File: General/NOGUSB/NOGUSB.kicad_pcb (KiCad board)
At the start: 2 copper layers, 34 parts, among them J1 USB4105-GF-A, J2 SPI/I2C/CAN/DAC, J3 CAN, J4 SWD_UART, SW1 RST, SW2 DBG2, SW3 BOOT0, SW4 DBG1, U1 MAX77596ETBB+, U2 TCAN330G, U3 STM32G0B1KxTxN

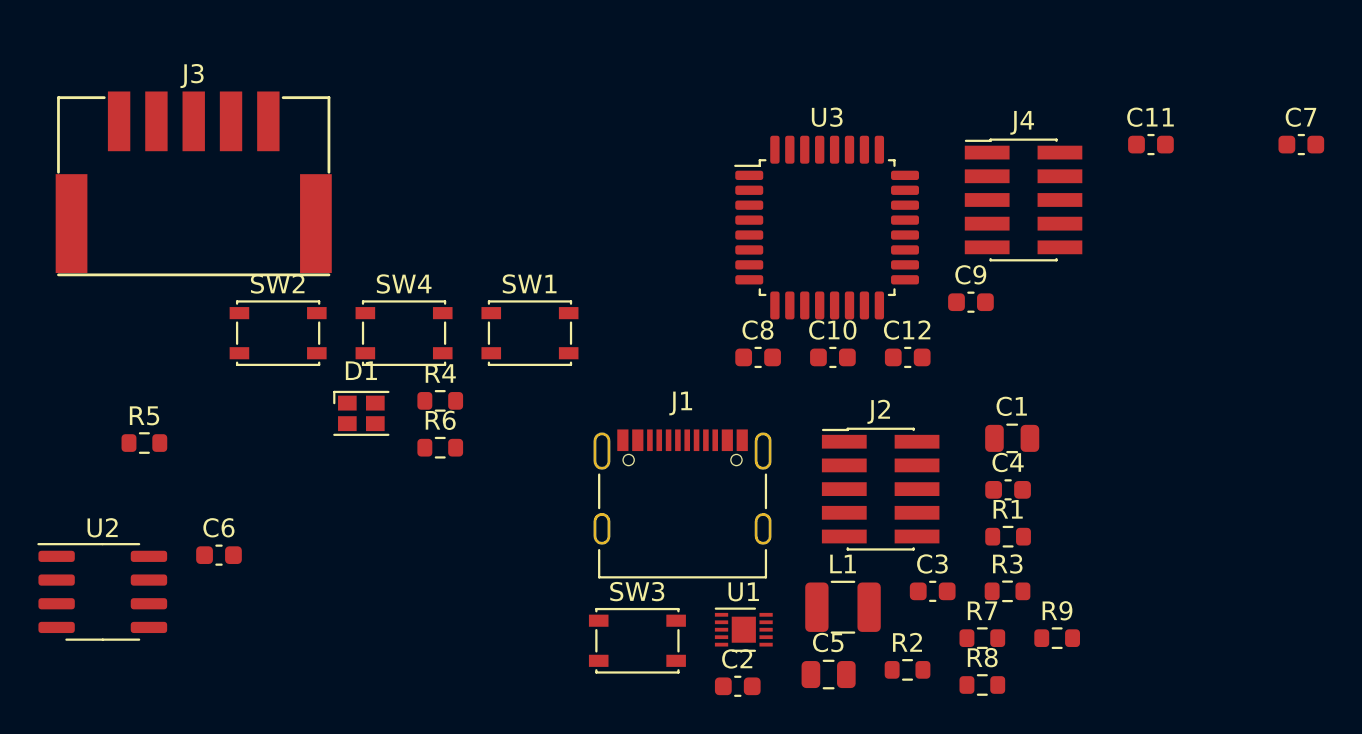
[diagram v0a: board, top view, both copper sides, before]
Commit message: finished NOGUSB layout
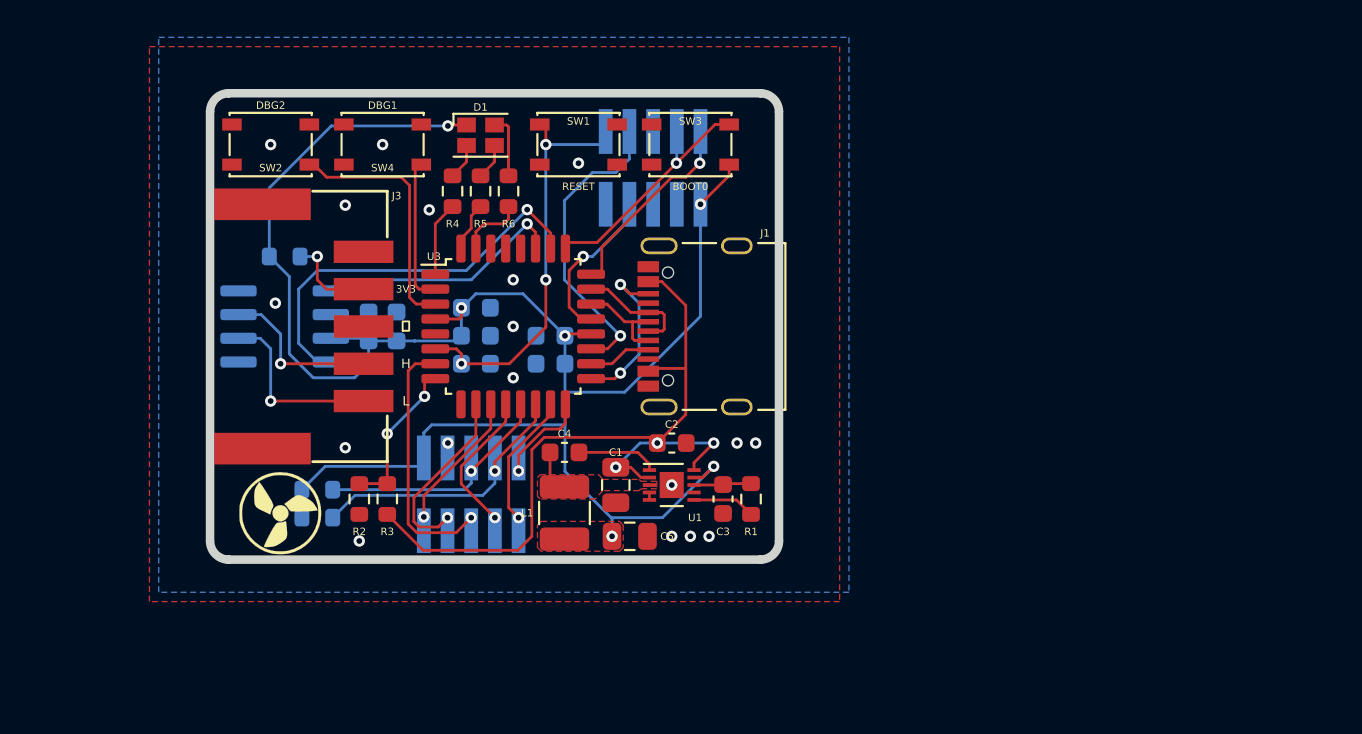
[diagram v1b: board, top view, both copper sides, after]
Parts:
- added H1: Logo, extraparts:auv_logo, F.Cu at (137.5, 110.0)
- C10, C11, C12, C6, C7, C8, C9, J2, J4, R7, R8, R9, U2: moved to B.Cu
- moved C7 49.5 mm to (143.8, 100.0), turned to 90 degrees
- moved R9 46.2 mm to (137.8, 96.2)
- moved R8 36.8 mm to (139.5, 110.2), turned to 180 degrees
- moved R7 36.5 mm to (139.5, 108.8), turned to 180 degrees
- moved R3 35.1 mm to (141.8, 109.2), turned to 270 degrees
- moved C11 33.8 mm to (152.0, 100.5), turned to 180 degrees
- moved R2 29.4 mm to (143.2, 109.2), turned to 90 degrees
- moved SW3 26.8 mm to (159.5, 90.2)
- moved C9 26.5 mm to (148.0, 99.0)
- moved C4 23.9 mm to (152.8, 106.8)
- moved R5 22.5 mm to (148.2, 92.8), turned to 90 degrees
- moved J2 22.0 mm to (147.8, 109.0), turned to 270 degrees
- moved C1 21.4 mm to (155.5, 108.5), turned to 270 degrees
- moved J4 19.9 mm to (157.5, 91.5), turned to 90 degrees
- moved C10 19.2 mm to (148.0, 100.5)
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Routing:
- net +3V3: track 0.00 -> 102.0 mm, vias 0 -> 6
- net VBUS: track 0.00 -> 43.0 mm, vias 0 -> 3
- net /RST: track 0.00 -> 21.7 mm, vias 0 -> 3
- net /CAN_RX: track 0.00 -> 21.7 mm, vias 0 -> 1
- net /NOGGIN/PA9(TX): track 0.00 -> 16.2 mm, vias 0 -> 1
- net /I2C_SCL: track 0.00 -> 15.3 mm, vias 0 -> 1
- net /SPI_CLK: track 0.00 -> 13.7 mm, vias 0 -> 1
- net /I2C_SDA: track 0.00 -> 13.6 mm, vias 0 -> 1
- net /CAN_TX: track 0.00 -> 13.5 mm, vias 0 -> 1
- net /BOOT0: track 0.00 -> 13.4 mm, vias 0 -> 1
- net /DBG2: track 0.00 -> 13.4 mm
- net /NOGGIN/PA13(SWDIO): track 0.00 -> 10.9 mm, vias 0 -> 1
- net /SPI_MISO: track 0.00 -> 9.80 mm, vias 0 -> 1
- net /CAN/CANL: track 0.00 -> 9.74 mm, vias 0 -> 1
- net /USB_CC2: track 0.00 -> 8.97 mm, vias 0 -> 2
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- added copper zone on F.Cu, net +3V3
- added copper zone on B.Cu, net GND
- added copper zone on F.Cu, net GND
- added copper zone on F.Cu, net Net-(C4-Pad1)
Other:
- board outline added: 30.5 x 25 mm
- board text added: "3V3"
- board text added: "BOOT0"
- board text added: "DBG1"
- board text added: "DBG2"
- board text added: "H"
- board text added: "L"
- board text added: "NOGUSB v1 Matthew Tran"
- board text added: "RESET"
- board text added: "SPI/I2C/CAN/DAC"
- board text added: "SWD/UART"
- board text added: "⏚"

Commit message: NOGUSB v1.1 revision
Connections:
- J4 pad 7: /NOGGIN/PA10(RX) -> /NOGGIN/PD2
- J4 pad 8: /NOGGIN/PA9(TX) -> /NOGGIN/PD3
- U3 pad 19: /NOGGIN/PA9(TX) -> /USB_CC1
- U3 pad 21: /NOGGIN/PA10(RX) -> /USB_CC2
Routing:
- net /NOGGIN/PA9(TX): track 16.2 -> 0.00 mm, vias 1 -> 0
- net /NOGGIN/PD3: track 0.00 -> 10.2 mm, vias 0 -> 1
- net /NOGGIN/PA10(RX): track 8.58 -> 0.00 mm, vias 1 -> 0
- net /NOGGIN/PD2: track 0.00 -> 8.57 mm, vias 0 -> 1
- net /RST: track 21.7 -> 22.9 mm
- net /USB_CC2: track 8.97 -> 9.99 mm, vias 2 -> 3
- net /USB_CC1: track 3.38 -> 4.18 mm
- net GND: vias 18 -> 24
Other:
- board text added: "NOGUSB v1.1 Matthew Tran"
- board text removed: "NOGUSB v1 Matthew Tran"

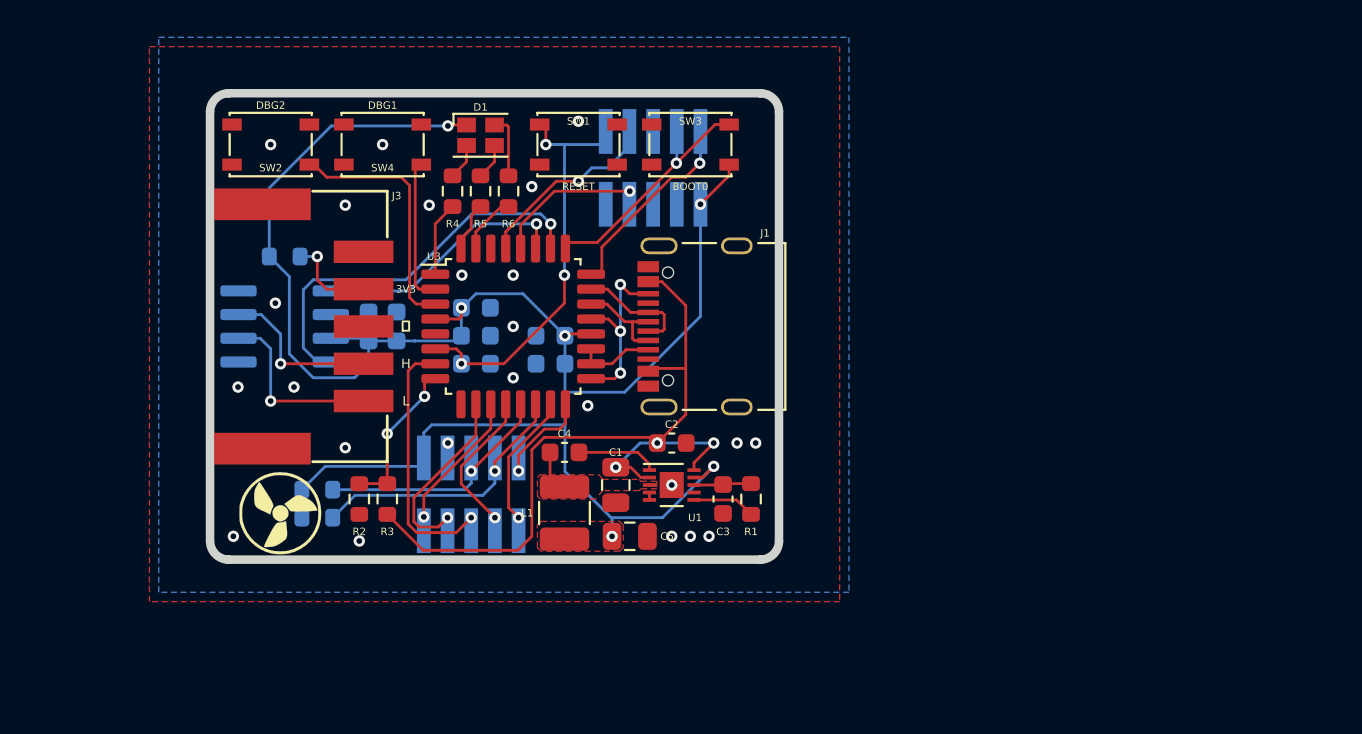
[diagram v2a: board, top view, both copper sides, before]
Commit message: convert to kicad 6
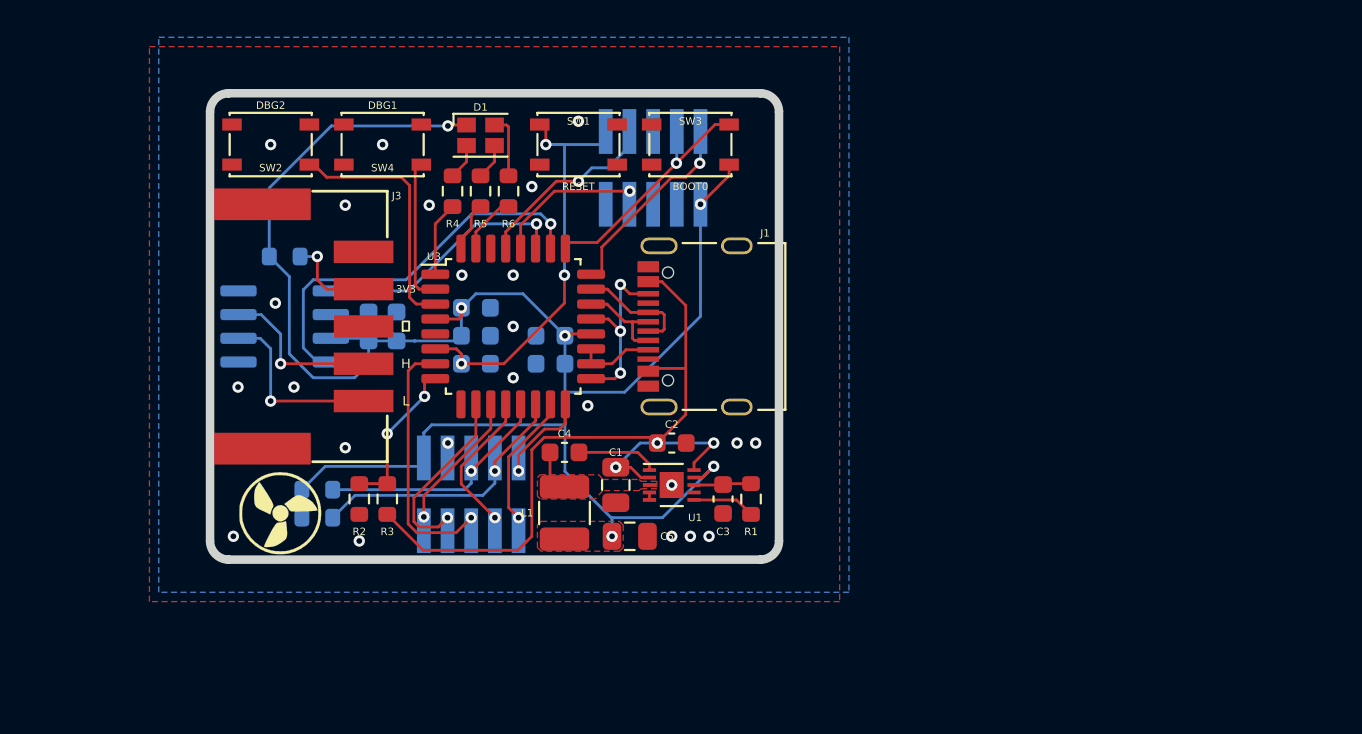
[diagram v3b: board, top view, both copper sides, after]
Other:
- net class Default removed
